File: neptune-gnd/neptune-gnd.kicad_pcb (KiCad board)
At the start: 4 copper layers, 30.5 x 60 mm, 23 parts, among them J1 Micro_SD_Card_Det2, J2 SMA, SW1 Boot Option, SW2 EN, U1 ESP32-S3-WROOM-1U, U2 AP2112K-3.3, U3 RFM95W-868S2

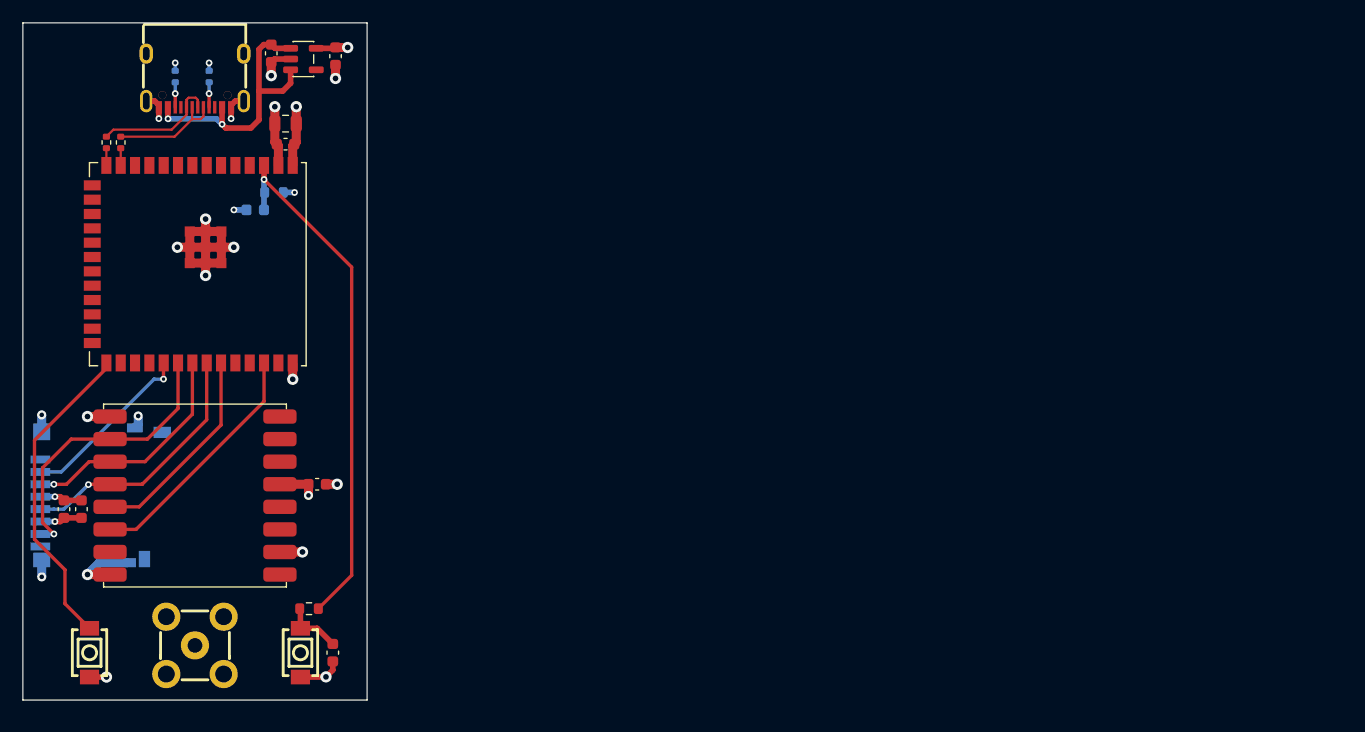
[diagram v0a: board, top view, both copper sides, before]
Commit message: fixing DRC problems, rerouting start
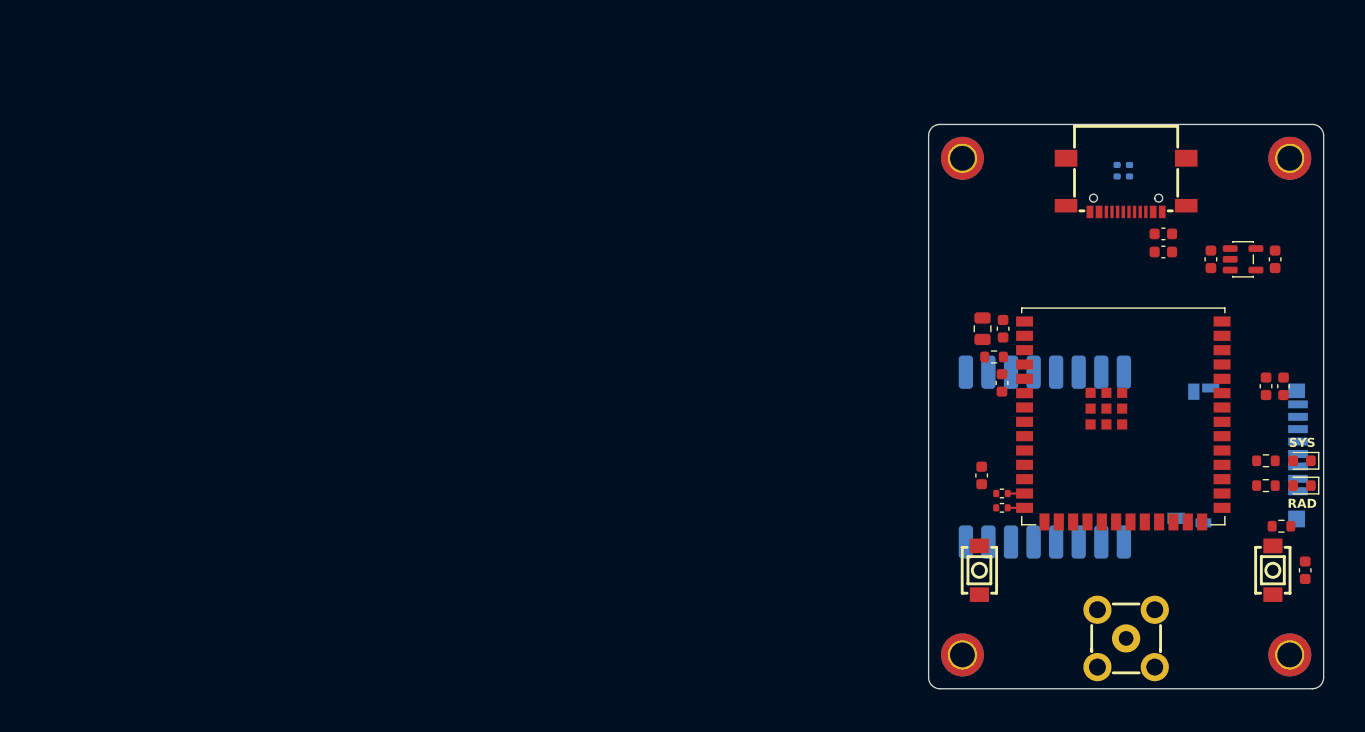
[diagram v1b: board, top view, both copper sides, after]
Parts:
- removed USB1: TYPE-C 16PIN 2MD(073), neptune-gnd:USB-C-SMD_TYPE-C-6PIN-2MD-073
- added C10: 100nF, Capacitor_SMD:C_0603_1608Metric, F.Cu at (191.2, 57.8)
- added C11: 10uF, Capacitor_SMD:C_0603_1608Metric, F.Cu at (191.2, 59.4)
- added D1: LED_Small, LED_SMD:LED_0603_1608Metric, F.Cu at (203.4, 80.1)
- added D2: LED_Small, LED_SMD:LED_0603_1608Metric, F.Cu at (203.4, 77.9)
- added H1: MountingHole, MountingHole:MountingHole_2.2mm_M2_DIN965_Pad_TopBottom, F.Cu at (202.4, 51.1)
- added H2: MountingHole, MountingHole:MountingHole_2.2mm_M2_DIN965_Pad_TopBottom, F.Cu at (173.4, 51.1)
- added H3: MountingHole, MountingHole:MountingHole_2.2mm_M2_DIN965_Pad_TopBottom, F.Cu at (173.4, 95.1)
- added H4: MountingHole, MountingHole:MountingHole_2.2mm_M2_DIN965_Pad_TopBottom, F.Cu at (202.4, 95.1)
- added J3: USB_C_Receptacle_USB2.0_16P, neptune-gnd:USB-SMD_TYPE-C-16PQT-073, F.Cu at (187.9, 53.5)
- added R3: 5.1k, Resistor_SMD:R_0402_1005Metric, B.Cu at (187.1, 52.2)
- added R4: 5.1k, Resistor_SMD:R_0402_1005Metric, B.Cu at (188.2, 52.2)
- C3, R1: moved to F.Cu
- R7, R8: value 5.1k -> 10k; footprint Resistor_SMD:R_0402_1005Metric -> Resistor_SMD:R_0603_1608Metric; moved to F.Cu
- U3: moved to B.Cu
- moved C5 108.6 mm to (201.8, 71.3), turned to 90 degrees
- moved C6 105.5 mm to (200.3, 71.3), turned to 90 degrees
- moved R7 102.5 mm to (200.2, 77.9), turned to 180 degrees
- moved J1 100.8 mm to (197.7, 77.4), turned to -90 degrees
- moved R8 100.4 mm to (200.2, 80.1), turned to 0 degrees
- moved R2 86.5 mm to (201.6, 83.7)
- moved SW2 86.5 mm to (200.9, 87.6)
- moved C4 86.5 mm to (203.7, 87.6)
- moved R6 85.7 mm to (176.9, 82.1), turned to 0 degrees
- moved C7 85.2 mm to (195.4, 60.1)
- moved C8 85.2 mm to (201.1, 60.1)
- moved U2 85.1 mm to (198.2, 60.1)
- moved R5 84.0 mm to (176.9, 80.8), turned to 0 degrees
- moved U1 83.1 mm to (187.6, 74.0), turned to 0 degrees
- moved J2 82.5 mm to (187.9, 93.7)
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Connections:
- R7 pad 2: GND -> Net-(U1-IO37)
- R8 pad 2: GND -> Net-(U1-IO36)
- U1 pad 29: unconnected-(U1-IO36-Pad29) -> Net-(U1-IO36)
- U1 pad 30: unconnected-(U1-IO37-Pad30) -> Net-(U1-IO37)
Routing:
- net GND: track 64.0 -> 0.00 mm, vias 23 -> 0
- net /EN: track 46.4 -> 0.00 mm, vias 1 -> 0
- net Net-(U1-IO0): track 28.2 -> 0.00 mm
- net /SPI_MISO: track 25.7 -> 0.00 mm, vias 1 -> 0
- net VCC: track 24.9 -> 0.00 mm, vias 2 -> 0
- net /SPI_CLK: track 23.1 -> 0.00 mm, vias 1 -> 0
- net /LORA_Reset: track 21.8 -> 0.00 mm
- net /SPI_MOSI: track 20.6 -> 0.00 mm, vias 1 -> 0
- net /CS_LORA: track 18.3 -> 0.00 mm
- net +3.3V: track 16.4 -> 0.00 mm, vias 5 -> 0
- net /SD_CS: track 15.8 -> 0.00 mm, vias 1 -> 0
- net /USB_DP: track 11.1 -> 0.00 mm
- net /USB_DM: track 9.92 -> 0.00 mm
- net Net-(C4-Pad1): track 5.21 -> 0.09 mm
- net Net-(D2-A): track 2.22 -> 0.00 mm, vias 1 -> 0
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- added copper zone on In1.Cu, net +3.3V
- added copper zone on In2.Cu, net GND
- removed copper zone on In2.Cu, net +3.3V
- removed copper zone on In1.Cu, net GND
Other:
- board size 30.5 x 60 mm -> 35 x 50 mm
- board text added: "RAD"
- board text added: "SYS"

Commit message: send to production
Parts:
- added R10: 10k, Resistor_SMD:R_0603_1608Metric, F.Cu at (177.5, 63.0)
- added R9: 10k, Resistor_SMD:R_0603_1608Metric, F.Cu at (177.5, 53.4)
- added SW3: SW_Slide_DPDT, neptune-gnd:MS-22D28-G020, F.Cu at (174.9, 58.3)
- C5, C6, C9: moved to B.Cu
- moved C4 32.3 mm to (171.7, 83.5), turned to 90 degrees
- moved R2 27.7 mm to (173.9, 84.3)
- moved SW1 27.5 mm to (202.4, 88.1)
- moved SW2 27.5 mm to (173.4, 88.1)
- moved C9 11.3 mm to (182.6, 87.7), turned to 0 degrees
- moved C11 7.02 mm to (197.1, 55.6), turned to -90 degrees
- moved C7 5.73 mm to (200.3, 57.1), turned to 0 degrees
- moved C10 4.83 mm to (195.5, 55.6), turned to 90 degrees
- moved C6 3.89 mm to (202.5, 68.1), turned to 180 degrees
- moved C8 2.85 mm to (200.3, 62.8), turned to 0 degrees
- moved U2 2.06 mm to (200.3, 60.0), turned to -90 degrees
- moved C5 1.77 mm to (202.5, 69.7), turned to 180 degrees
- moved U1 0.72 mm to (188.3, 73.9)
- turned R8 to 180 degrees
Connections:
- C10 pad 1: VBUS -> VCC
- C11 pad 2: VBUS -> VCC
- J3 pad A4B9: VBUS -> VCC
- J3 pad A6: Net-(J3-D+-PadA6) -> /USB_DP
- J3 pad A7: Net-(J3-D--PadA7) -> /USB_DN
- J3 pad B4A9: VBUS -> VCC
- J3 pad B6: Net-(J3-D+-PadA6) -> /USB_DP
- J3 pad B7: Net-(J3-D--PadA7) -> /USB_DN
- R5 pad 1: /USB_DM -> /USB_DN
- U1 pad 4: unconnected-(U1-IO4-Pad4) -> Net-(U1-IO4)
- U1 pad 5: unconnected-(U1-IO5-Pad5) -> Net-(U1-IO5)
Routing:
- net GND: track 0.00 -> 94.4 mm, vias 0 -> 32
- net /USB_DN: track 0.00 -> 46.2 mm, vias 0 -> 2
- net /USB_DP: track 0.00 -> 44.1 mm, vias 0 -> 2
- net +3.3V: track 0.00 -> 33.2 mm, vias 0 -> 5
- net /SPI_MISO: track 0.00 -> 31.9 mm, vias 0 -> 2
- net /SPI_MOSI: track 0.00 -> 31.1 mm, vias 0 -> 2
- net /SPI_CLK: track 0.00 -> 27.3 mm, vias 0 -> 2
- net VCC: track 0.00 -> 22.6 mm
- net Net-(U1-IO5): track 0.00 -> 20.1 mm
- net /EN: track 0.00 -> 19.8 mm
- net /CS_LORA: track 0.00 -> 16.8 mm, vias 0 -> 1
- net /LORA_Reset: track 0.00 -> 15.5 mm, vias 0 -> 1
- net Net-(U1-IO4): track 0.00 -> 9.48 mm
- net Net-(U1-IO0): track 0.00 -> 8.74 mm
- net /RX: track 0.00 -> 8.69 mm
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- added copper zone on B.Cu, net GND
- added copper zone on F.Cu, net GND
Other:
- board text added: "BOOT"
- board text added: "CPWR"
- board text added: "Follow us on Social Media"
- board text added: "Ground Station"
- board text added: "RX"
- board text added: "TX"
- board text added: "revision 1.0 Project Neptune"

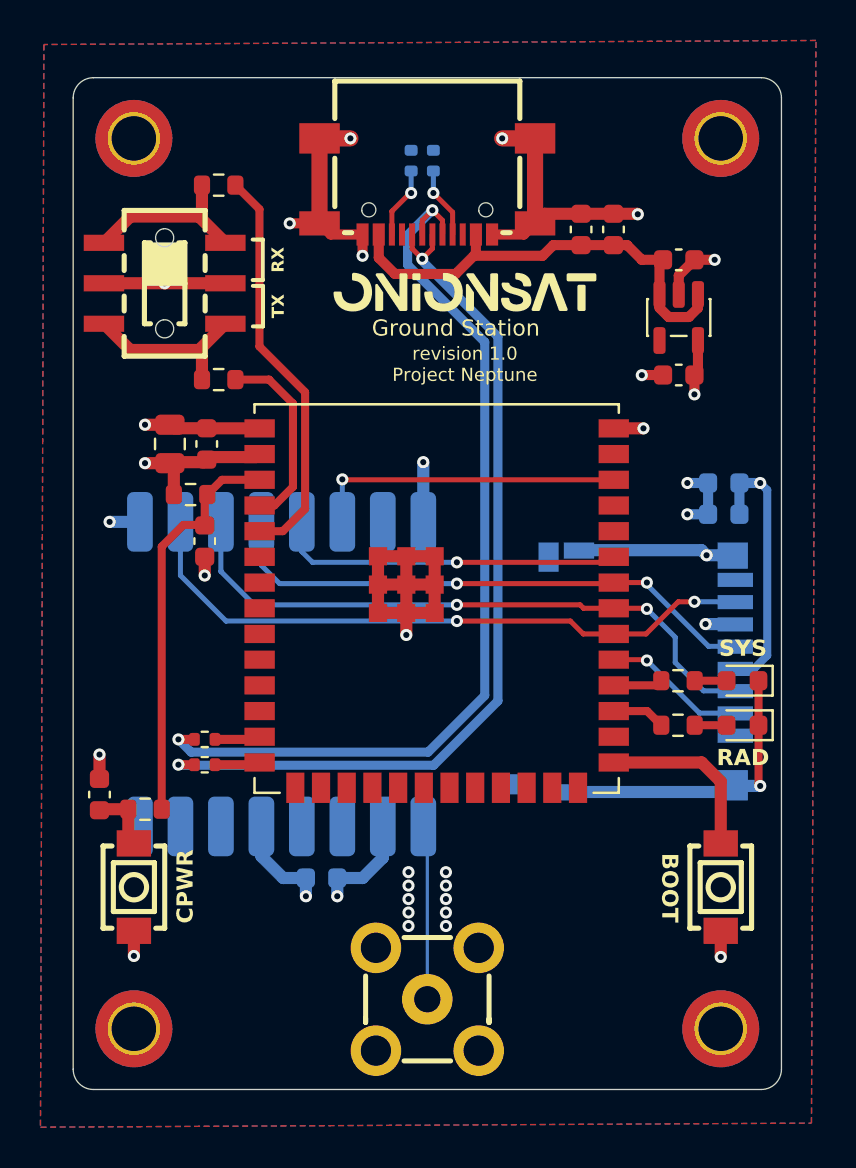
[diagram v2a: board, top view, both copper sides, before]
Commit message: v1.1 - adding interrupt conn
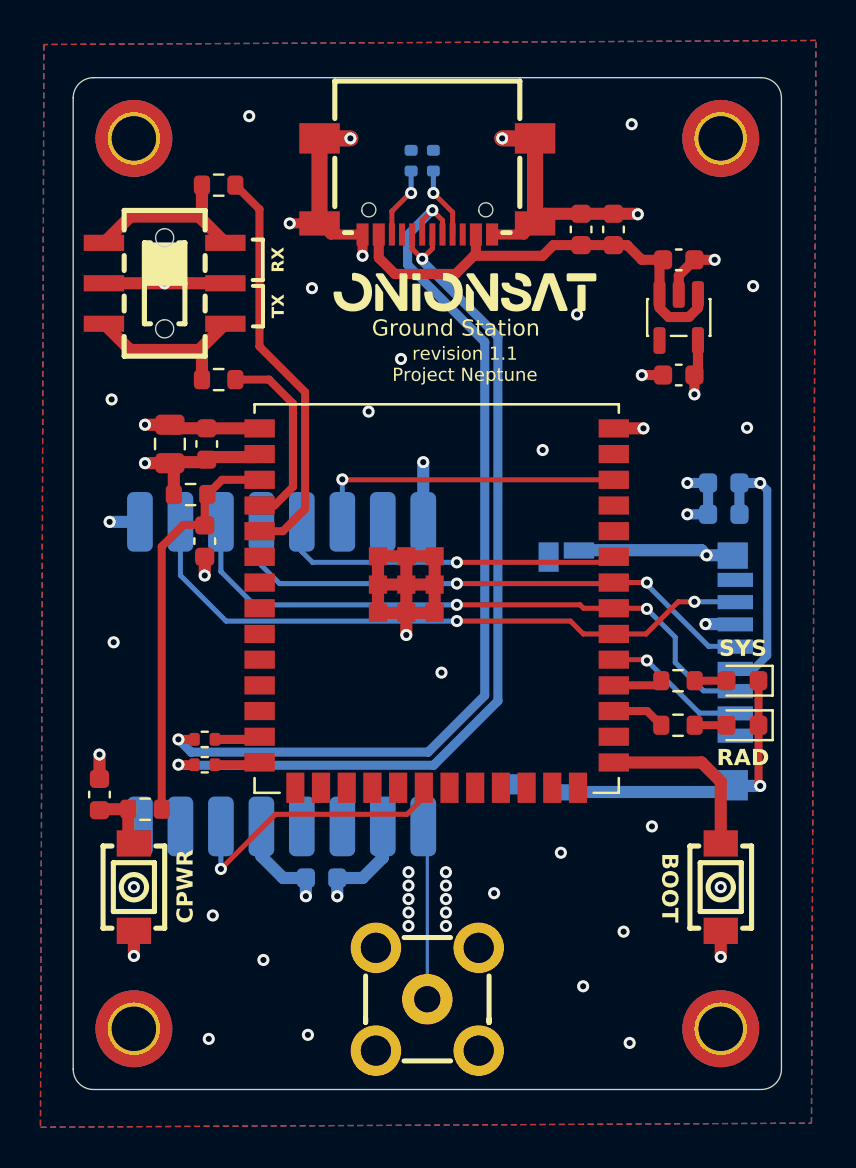
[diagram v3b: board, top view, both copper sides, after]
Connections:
- U1 pad 20: unconnected-(U1-IO12-Pad20) -> /LORA_DIO0
- U3 pad 14: unconnected-(U3-DIO0-Pad14) -> /LORA_DIO0
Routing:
- net /LORA_DIO0: track 0.00 -> 14.1 mm, vias 0 -> 1
- net GND: vias 32 -> 56
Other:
- board text added: "revision 1.1 Project Neptune"

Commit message: silkscreen fix ver number
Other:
- board text removed: "revision 1.0 Project Neptune"
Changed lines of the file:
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@@
 		)
 	)
-	(gr_text "revision 1.0\nProject Neptune\n\n"
+	(gr_text "revision 1.1\nProject Neptune\n\n"
 		(at 195.543 77.441869 270)
 		(layer "B.SilkS")
@@
 		)
 	)
-	(group ""
-		(members "126f9a6d-5908-46c5-ba39-5b4b2d5a7cf4" "4c59ddaf-7f34-4d4f-9444-8f3cf243aee1"
-			"a3982acf-ccbf-485c-ac49-f5d2914e9333"
-		)
-	)
